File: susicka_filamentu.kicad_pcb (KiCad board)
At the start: 2 copper layers, 6 parts, among them J2 Conn_01x03, J4 PJ-102AH, U1 RP2350A-QFN60, U2 RM2, U3 W25Q128JVS

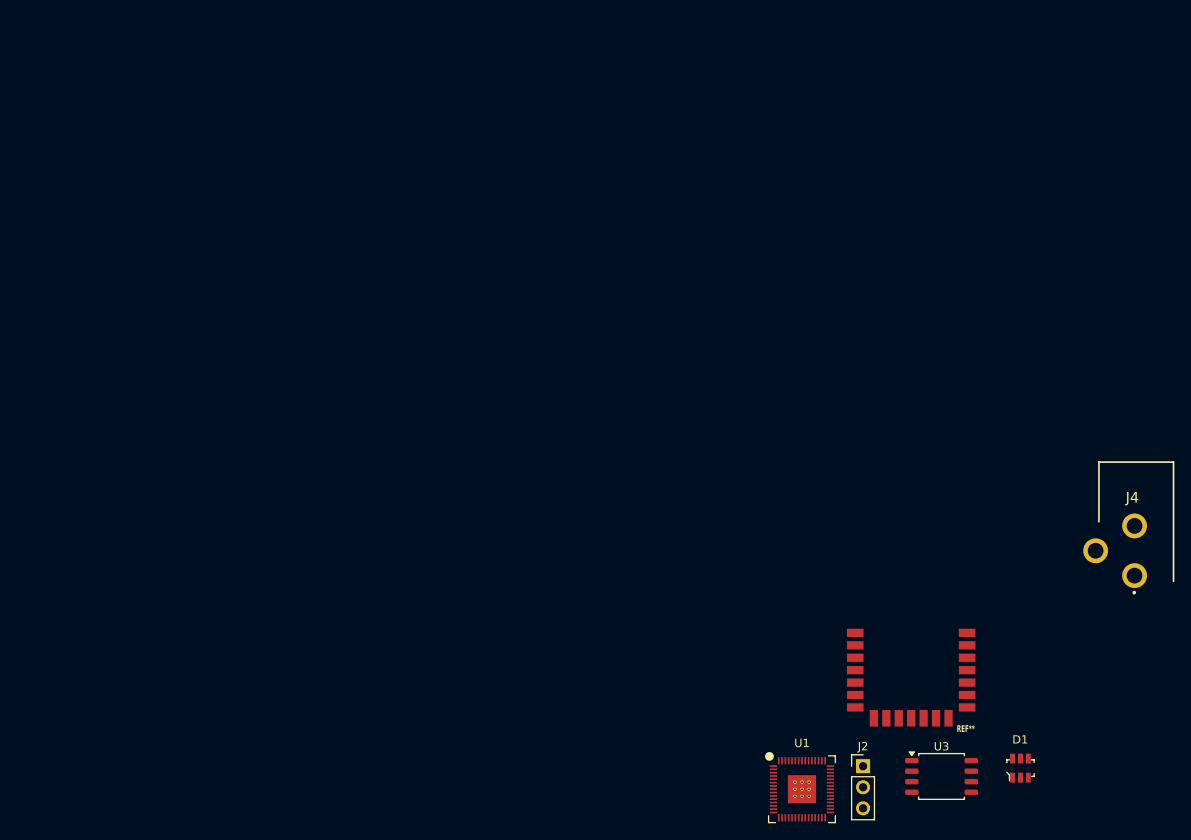
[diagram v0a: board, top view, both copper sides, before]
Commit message: feat(pcb): 4-layer stackup configuration, floorplan placement of RP2350A, RM2, sensors, MOSFET heater control, 85x65mm Edge.Cuts, and +3.3V/GND copper planes
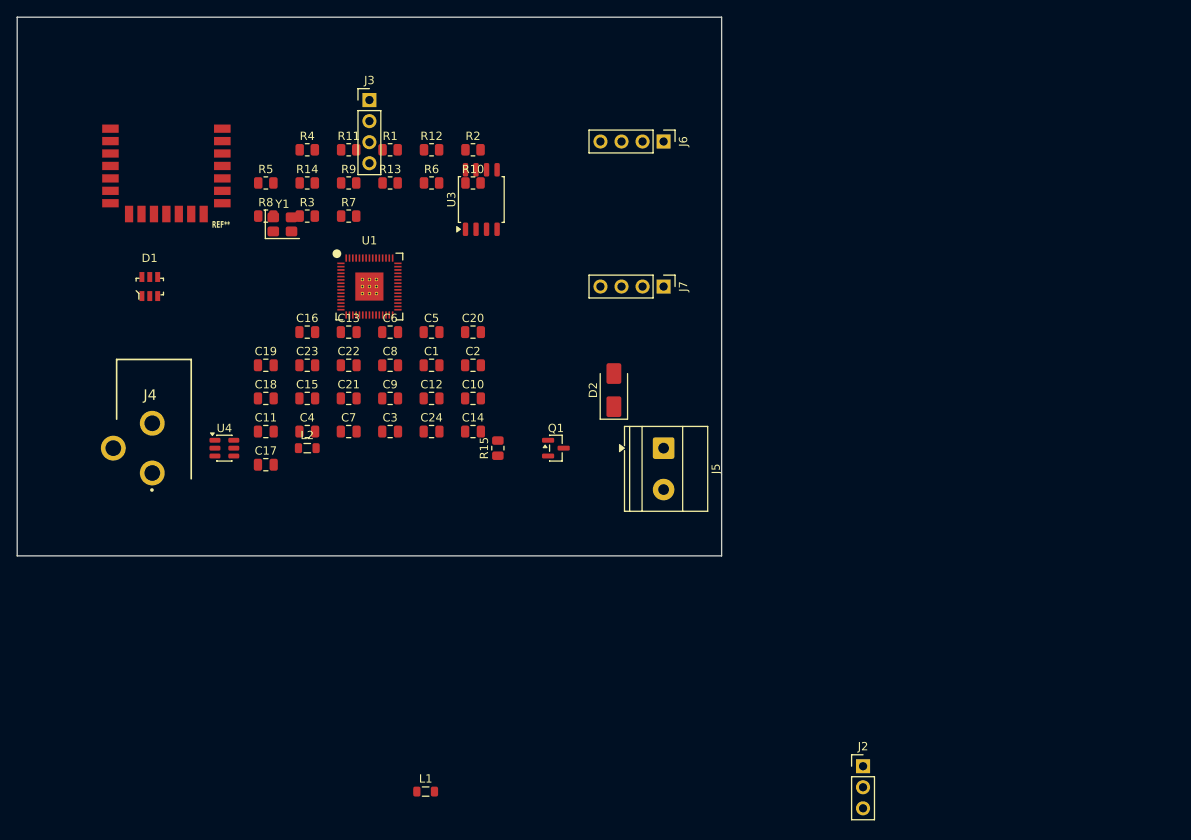
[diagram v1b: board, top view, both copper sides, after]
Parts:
- added C1: 15p, Capacitor_SMD:C_0805_2012Metric, F.Cu at (50.0, 42.0)
- added C10: 100 nF, Capacitor_SMD:C_0805_2012Metric, F.Cu at (55.0, 46.0)
- added C11: 100 nF, Capacitor_SMD:C_0805_2012Metric, F.Cu at (30.0, 50.0)
- added C12: 100 nF, Capacitor_SMD:C_0805_2012Metric, F.Cu at (50.0, 46.0)
- added C13: 100 nF, Capacitor_SMD:C_0805_2012Metric, F.Cu at (40.0, 38.0)
- added C14: 100 nF, Capacitor_SMD:C_0805_2012Metric, F.Cu at (55.0, 50.0)
- added C15: 100 nF, Capacitor_SMD:C_0805_2012Metric, F.Cu at (35.0, 46.0)
- added C16: 4,7 uF, Capacitor_SMD:C_0805_2012Metric, F.Cu at (35.0, 38.0)
- added C17: 100 nF, Capacitor_SMD:C_0805_2012Metric, F.Cu at (30.0, 54.0)
- added C18: 100 nF, Capacitor_SMD:C_0805_2012Metric, F.Cu at (30.0, 46.0)
- added C19: 10 uF, Capacitor_SMD:C_0805_2012Metric, F.Cu at (30.0, 42.0)
- added C2: 15p, Capacitor_SMD:C_0805_2012Metric, F.Cu at (55.0, 42.0)
- added C20: 100 nF, Capacitor_SMD:C_0805_2012Metric, F.Cu at (55.0, 38.0)
- added C21: 10 uF, Capacitor_SMD:C_0805_2012Metric, F.Cu at (40.0, 46.0)
- added C22: 100 nF, Capacitor_SMD:C_0805_2012Metric, F.Cu at (40.0, 42.0)
- added C23: 22 uF, Capacitor_SMD:C_0805_2012Metric, F.Cu at (35.0, 42.0)
- added C24: 22 uF, Capacitor_SMD:C_0805_2012Metric, F.Cu at (50.0, 50.0)
- added C3: 4,7n, Capacitor_SMD:C_0805_2012Metric, F.Cu at (45.0, 50.0)
- added C4: 4,7uF, Capacitor_SMD:C_0805_2012Metric, F.Cu at (35.0, 50.0)
- added C5: 4,7 uF, Capacitor_SMD:C_0805_2012Metric, F.Cu at (50.0, 38.0)
- added C6: 4,7 uF, Capacitor_SMD:C_0805_2012Metric, F.Cu at (45.0, 38.0)
- added C7: 100 nF, Capacitor_SMD:C_0805_2012Metric, F.Cu at (40.0, 50.0)
- added C8: 100 nF, Capacitor_SMD:C_0805_2012Metric, F.Cu at (45.0, 42.0)
- added C9: 100 nF, Capacitor_SMD:C_0805_2012Metric, F.Cu at (45.0, 46.0)
- added D2: SS14, Diode_SMD:D_SMA, F.Cu at (72.0, 45.0)
- added J3: Conn_01x04, Connector_PinHeader_2.54mm:PinHeader_1x04_P2.54mm_Vertical, F.Cu at (42.5, 10.0)
- added J5: Screw_Terminal_01x02, TerminalBlock_Phoenix:TerminalBlock_Phoenix_MKDS-1,5-2_1x02_P5.00mm_Horizontal, F.Cu at (78.0, 52.0)
- added J6: Conn_01x04, Connector_PinHeader_2.54mm:PinHeader_1x04_P2.54mm_Vertical, F.Cu at (78.0, 15.0)
- added J7: Conn_01x04, Connector_PinHeader_2.54mm:PinHeader_1x04_P2.54mm_Vertical, F.Cu at (78.0, 32.5)
- added L1: AOTA-B201610S3R3-101-T, Inductor_SMD:L_0805_2012Metric, F.Cu at (49.3, 93.4)
- added L2: 3,9 uH, Inductor_SMD:L_0805_2012Metric, F.Cu at (35.0, 52.0)
- added Q1: Q_NMOS_GSD, Package_TO_SOT_SMD:SOT-23, F.Cu at (65.0, 52.0)
- added R1: 1k, Resistor_SMD:R_0805_2012Metric, F.Cu at (45.0, 16.0)
- added R10: 10k, Resistor_SMD:R_0805_2012Metric, F.Cu at (55.0, 20.0)
- added R11: 10k, Resistor_SMD:R_0805_2012Metric, F.Cu at (40.0, 16.0)
- added R12: 10k, Resistor_SMD:R_0805_2012Metric, F.Cu at (50.0, 16.0)
- added R13: 10k, Resistor_SMD:R_0805_2012Metric, F.Cu at (45.0, 20.0)
- added R14: 470, Resistor_SMD:R_0805_2012Metric, F.Cu at (35.0, 20.0)
- added R15: R, Resistor_SMD:R_0805_2012Metric, F.Cu at (58.0, 52.0)
- added R2: 5,1k, Resistor_SMD:R_0805_2012Metric, F.Cu at (55.0, 16.0)
- added R3: 5,1k, Resistor_SMD:R_0805_2012Metric, F.Cu at (35.0, 24.0)
- added R4: 27, Resistor_SMD:R_0805_2012Metric, F.Cu at (35.0, 16.0)
- added R5: 27, Resistor_SMD:R_0805_2012Metric, F.Cu at (30.0, 20.0)
- added R6: 1M, Resistor_SMD:R_0805_2012Metric, F.Cu at (50.0, 20.0)
- added R7: 33, Resistor_SMD:R_0805_2012Metric, F.Cu at (40.0, 24.0)
- added R8: 220, Resistor_SMD:R_0805_2012Metric, F.Cu at (30.0, 24.0)
- added R9: 220, Resistor_SMD:R_0805_2012Metric, F.Cu at (40.0, 20.0)
- added U4: AP63203WU, Package_TO_SOT_SMD:TSOT-23-6, F.Cu at (25.0, 52.0)
- added Y1: Crystal_GND24, Crystal:Crystal_SMD_3225-4Pin_3.2x2.5mm, F.Cu at (32.0, 25.0)
- moved D1 120.1 mm to (16.0, 32.5)
- moved J4 119.2 mm to (12.0, 52.0)
- moved U2 108.5 mm to (18.0, 16.0)
- moved U3 89.1 mm to (56.0, 22.0), turned to 90 degrees
- moved U1 80.0 mm to (42.5, 32.5)
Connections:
- D1 pad 2: GND -> +3V3
- J2 pad 3: GND -> +3V3
- J4 pad 1: unconnected-(J4-Pad1) -> 24V
- J4 pad 2: unconnected-(J4-Pad2) -> +3V3
- J4 pad 3: unconnected-(J4-Pad3) -> +3V3
- U1 pad 18: unconnected-(U1-GPIO14-Pad18) -> /GPIO14
- U1 pad 4: unconnected-(U1-GPIO2-Pad4) -> Net-(J6-Pin_3)
- U1 pad 47: GND -> +3V3
- U1 pad 5: unconnected-(U1-GPIO3-Pad5) -> Net-(J6-Pin_4)
- U1 pad 61: GND -> +3V3
- U1 pad 7: unconnected-(U1-GPIO4-Pad7) -> Net-(J7-Pin_3)
- U1 pad 8: unconnected-(U1-GPIO5-Pad8) -> Net-(J7-Pin_4)
- U2 pad 1: GND -> +3V3
- U2 pad 11: GND -> +3V3
- U2 pad 15: GND -> +3V3
- U2 pad 21: GND -> +3V3
- U2 pad 4: GND -> +3V3
- U2 pad 7: GND -> +3V3
- U3 pad 4: GND -> +3V3
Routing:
- added copper zone on In2.Cu, net +3V3
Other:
- board outline added: 85 x 65 mm
- copper layers 2 -> 4

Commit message: feat(pcb): Senior PCB Layout & Routing: enforce RF antenna Keepout zone, place MCU & decoupling caps adjacent to VDD, route power/GND vias, and generate +3V3/GND copper planes
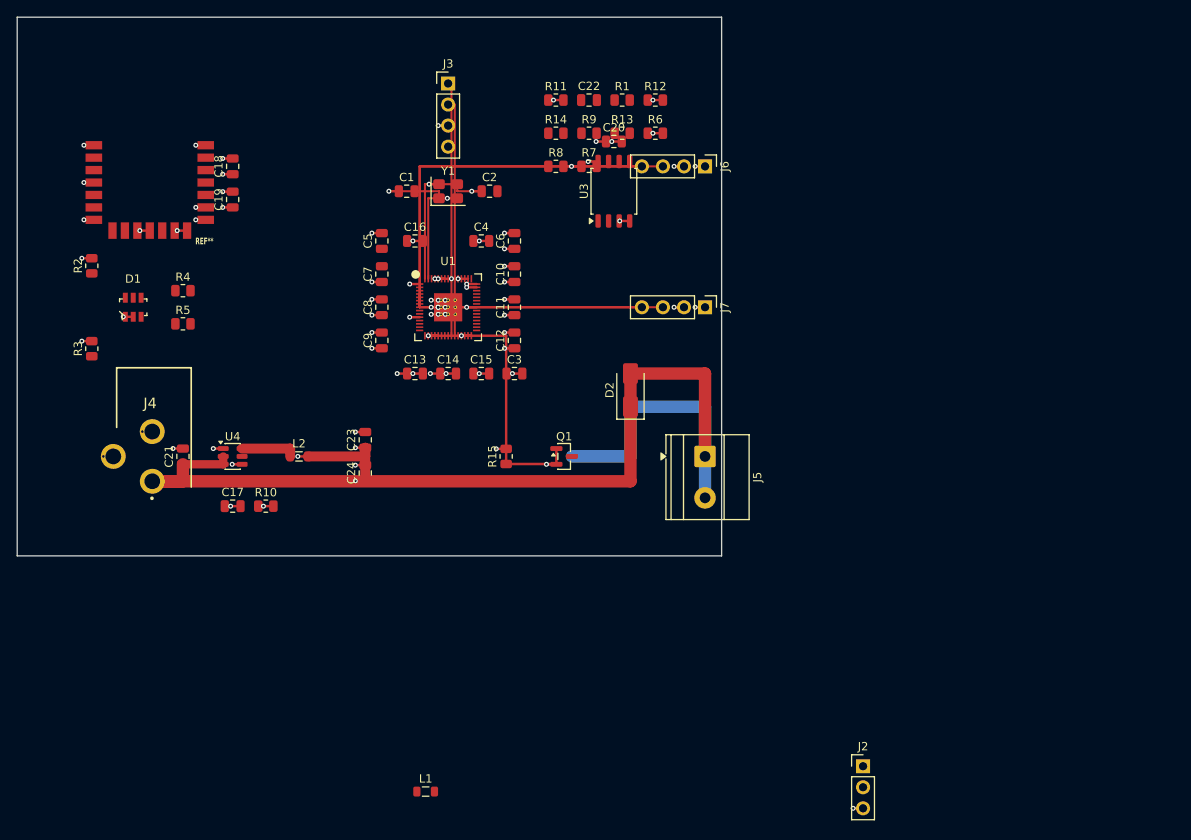
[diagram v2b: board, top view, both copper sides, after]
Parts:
- moved R2 48.1 mm to (9.00, 30.0), turned to 90 degrees
- moved R10 46.3 mm to (30.0, 59.0)
- moved C22 43.2 mm to (69.0, 10.0)
- moved R8 35.5 mm to (65.0, 18.0)
- moved C11 33.5 mm to (60.0, 35.0), turned to 90 degrees
- moved C4 31.1 mm to (56.0, 27.0)
- moved R14 30.6 mm to (65.0, 14.0)
- moved R3 30.5 mm to (9.00, 40.0), turned to 90 degrees
- moved R7 29.6 mm to (69.0, 18.0)
- moved R9 29.6 mm to (69.0, 14.0)
- moved R1 28.6 mm to (73.0, 10.0)
- moved R13 28.6 mm to (73.0, 14.0)
- moved C20 28.6 mm to (72.0, 15.0)
- moved C18 28.3 mm to (26.0, 18.0), turned to 90 degrees
- moved R12 27.7 mm to (77.0, 10.0)
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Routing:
- net +3V3: track 0.00 -> 129.5 mm, vias 0 -> 90
- net 24V: track 0.00 -> 82.3 mm
- net Net-(J6-Pin_3): track 0.00 -> 46.0 mm
- net Net-(J6-Pin_4): track 0.00 -> 43.8 mm
- net (no net): track 0.00 -> 39.0 mm
- net /GPIO14: track 0.00 -> 32.4 mm
- net Net-(J7-Pin_3): track 0.00 -> 31.0 mm
- net SWDIO: track 0.00 -> 30.8 mm
- net SWCLK: track 0.00 -> 28.7 mm
- net Net-(J7-Pin_4): track 0.00 -> 28.0 mm
- net /oscillator/XIN: track 0.00 -> 15.3 mm
- net Net-(J5-Pin_2): track 0.00 -> 13.1 mm
- net Net-(C2-Pad2): track 0.00 -> 11.0 mm
- net Net-(U4-BST): track 0.00 -> 6.75 mm

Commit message: Complete senior 4-layer PCB layout & routing with 0 DRC errors and full keepout enforcement
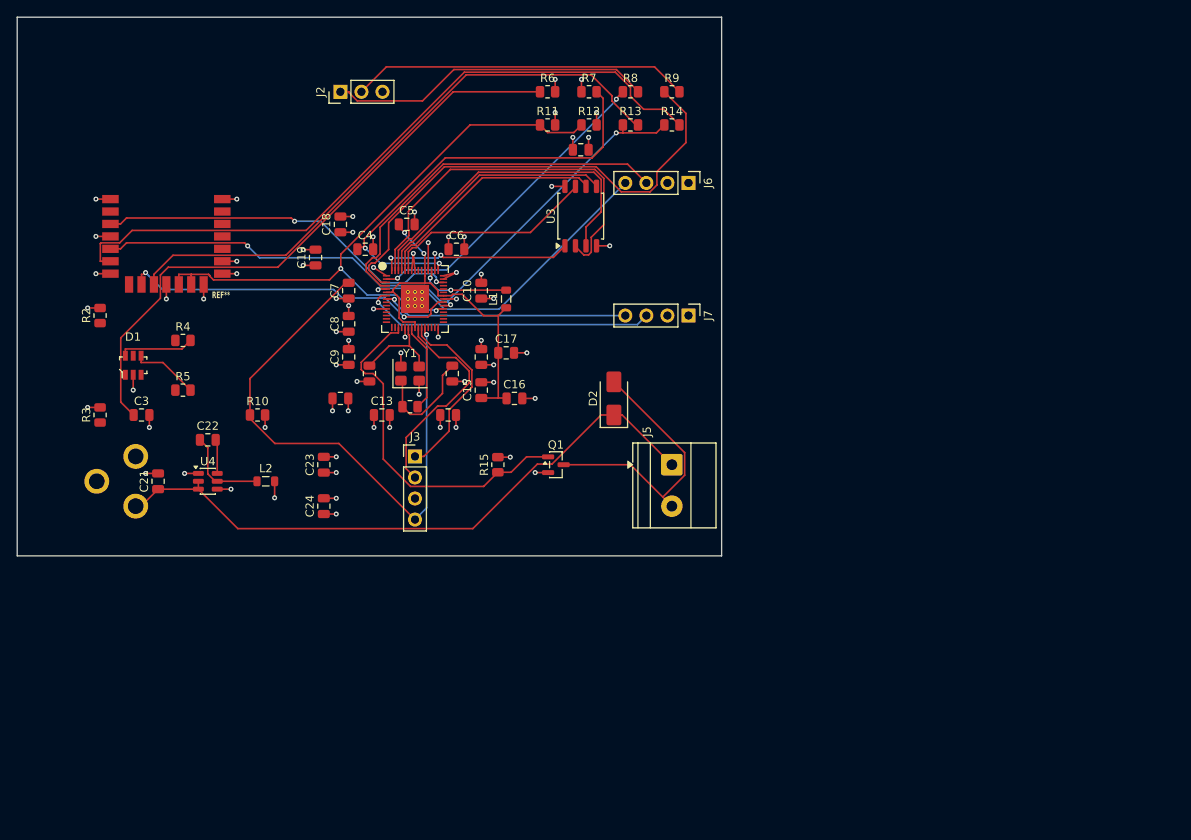
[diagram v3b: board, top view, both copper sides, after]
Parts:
- moved J2 103.0 mm to (39.0, 9.00), turned to 90 degrees
- moved C22 61.6 mm to (23.0, 51.0)
- moved L1 60.2 mm to (59.0, 34.0), turned to 90 degrees
- moved C3 45.3 mm to (15.0, 48.0)
- moved J3 45.2 mm to (48.0, 53.0)
- moved R1 45.0 mm to (47.4, 47.0)
- moved C17 37.8 mm to (59.0, 40.5)
- moved Y1 22.5 mm to (47.4, 43.0)
- moved C16 22.5 mm to (60.0, 46.0)
- moved C1 22.5 mm to (42.5, 43.0), turned to 90 degrees
- moved C2 22.5 mm to (52.5, 43.0), turned to 90 degrees
- moved C12 22.1 mm to (39.0, 46.0), turned to 0 degrees
- moved C18 14.8 mm to (39.0, 25.0)
- moved C4 14.0 mm to (42.0, 28.0)
- moved R14 14.0 mm to (79.0, 13.0)
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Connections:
- C1 pad 1: +3V3 -> GND
- C10 pad 2: +3V3 -> GND
- C11 pad 2: +3V3 -> GND
- C12 pad 2: +3V3 -> GND
- C13 pad 2: +3V3 -> GND
- C14 pad 2: +3V3 -> GND
- C15 pad 2: +3V3 -> GND
- C16 pad 2: +3V3 -> GND
- C17 pad 2: +3V3 -> GND
- C18 pad 2: +3V3 -> GND
- C19 pad 2: +3V3 -> GND
- C2 pad 1: +3V3 -> GND
- C20 pad 2: +3V3 -> GND
- C21 pad 2: +3V3 -> GND
- C23 pad 2: +3V3 -> GND
- C24 pad 2: +3V3 -> GND
- C3 pad 2: +3V3 -> GND
- C4 pad 2: +3V3 -> GND
- C5 pad 2: +3V3 -> GND
- C6 pad 2: +3V3 -> GND
- C7 pad 1: +3V3 -> GND
- C8 pad 2: +3V3 -> GND
- C9 pad 2: +3V3 -> GND
- D1 pad 2: +3V3 -> GND
- D2 pad 1: (no net) -> 24V
- D2 pad 2: (no net) -> Net-(J5-Pin_2)
- J2 pad 3: +3V3 -> GND
- J3 pad 3: +3V3 -> GND
- J4 pad 2: +3V3 -> GND
- J4 pad 3: +3V3 -> GND
- J6 pad 2: +3V3 -> GND
- J7 pad 1: +3V3 -> GND
- J7 pad 2: +3V3 -> unconnected-(J7-Pin_2-Pad2)
- Q1 pad 2: +3V3 -> GND
- R11 pad 2: +3V3 -> GND
- R12 pad 2: +3V3 -> GND
- R15 pad 2: +3V3 -> GND
- R2 pad 2: +3V3 -> GND
- R3 pad 2: +3V3 -> GND
- R6 pad 2: +3V3 -> GND
- U1 pad 47: +3V3 -> GND
- U1 pad 61: +3V3 -> GND
- U2 pad 1: +3V3 -> GND
- U2 pad 11: +3V3 -> GND
- U2 pad 15: +3V3 -> GND
- U2 pad 20: unconnected-(U2-NC-Pad20) -> (no net)
- U2 pad 21: +3V3 -> GND
- U2 pad 4: +3V3 -> GND
- U2 pad 7: +3V3 -> GND
- U3 pad 4: +3V3 -> GND
- U4 pad 4: +3V3 -> GND
- Y1 pad 2: +3V3 -> GND
- Y1 pad 4: +3V3 -> GND
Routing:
- net Net-(U2-DO): track 0.00 -> 85.1 mm
- net /RM2/RM2_DI: track 0.00 -> 81.3 mm, vias 0 -> 3
- net +3V3: track 129.5 -> 49.4 mm, vias 90 -> 28
- net /RM2/RM2_BT_ON: track 0.00 -> 75.8 mm, vias 0 -> 2
- net Net-(J1-SHIELD): track 0.00 -> 74.5 mm
- net Net-(U2-nIRQ): track 0.00 -> 72.5 mm
- net Net-(J3-Pin_4): track 0.00 -> 70.3 mm, vias 0 -> 1
- net GND: track 0.00 -> 64.5 mm, vias 0 -> 42
- net Net-(U1-GPIO1): track 0.00 -> 60.3 mm
- net Net-(U1-VREG_AVDD): track 0.00 -> 53.1 mm, vias 0 -> 2
- net /flash/QSPI_SD1: track 0.00 -> 46.1 mm
- net +1V1: track 0.00 -> 45.2 mm, vias 0 -> 2
- net /RM2/RM2_SCLK: track 0.00 -> 44.9 mm, vias 0 -> 2
- net /RM2/RM2_CS: track 0.00 -> 41.0 mm, vias 0 -> 2
- net Net-(J2-Pin_2): track 0.00 -> 40.9 mm
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- added copper zone on In1.Cu, net GND
